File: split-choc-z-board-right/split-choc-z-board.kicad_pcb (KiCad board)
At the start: 2 copper layers, 147.1 x 106.5 mm, 79 parts, among them J1 USB4105-GF-A, J2 USB4105-GF-A, SW1 SW_SPST, SW10 SW_SPST, SW11 SW_SPST, SW12 SW_SPST, SW13 SW_SPST, SW14 SW_SPST, SW15 SW_SPST, SW16 SW_SPST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

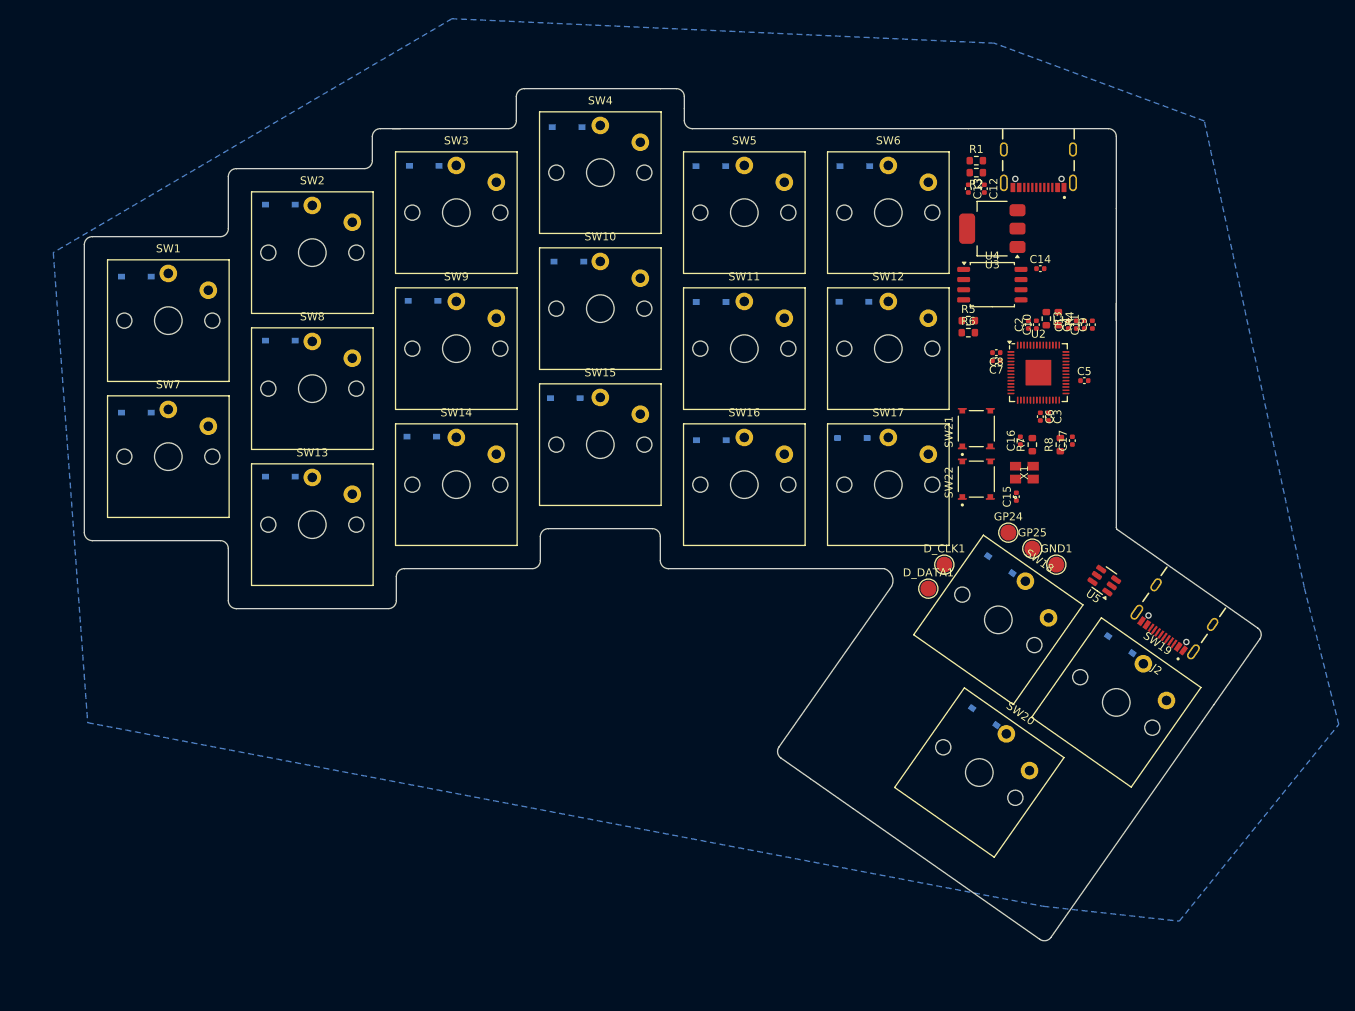
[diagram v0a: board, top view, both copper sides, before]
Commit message: Finalized component placement! 💡
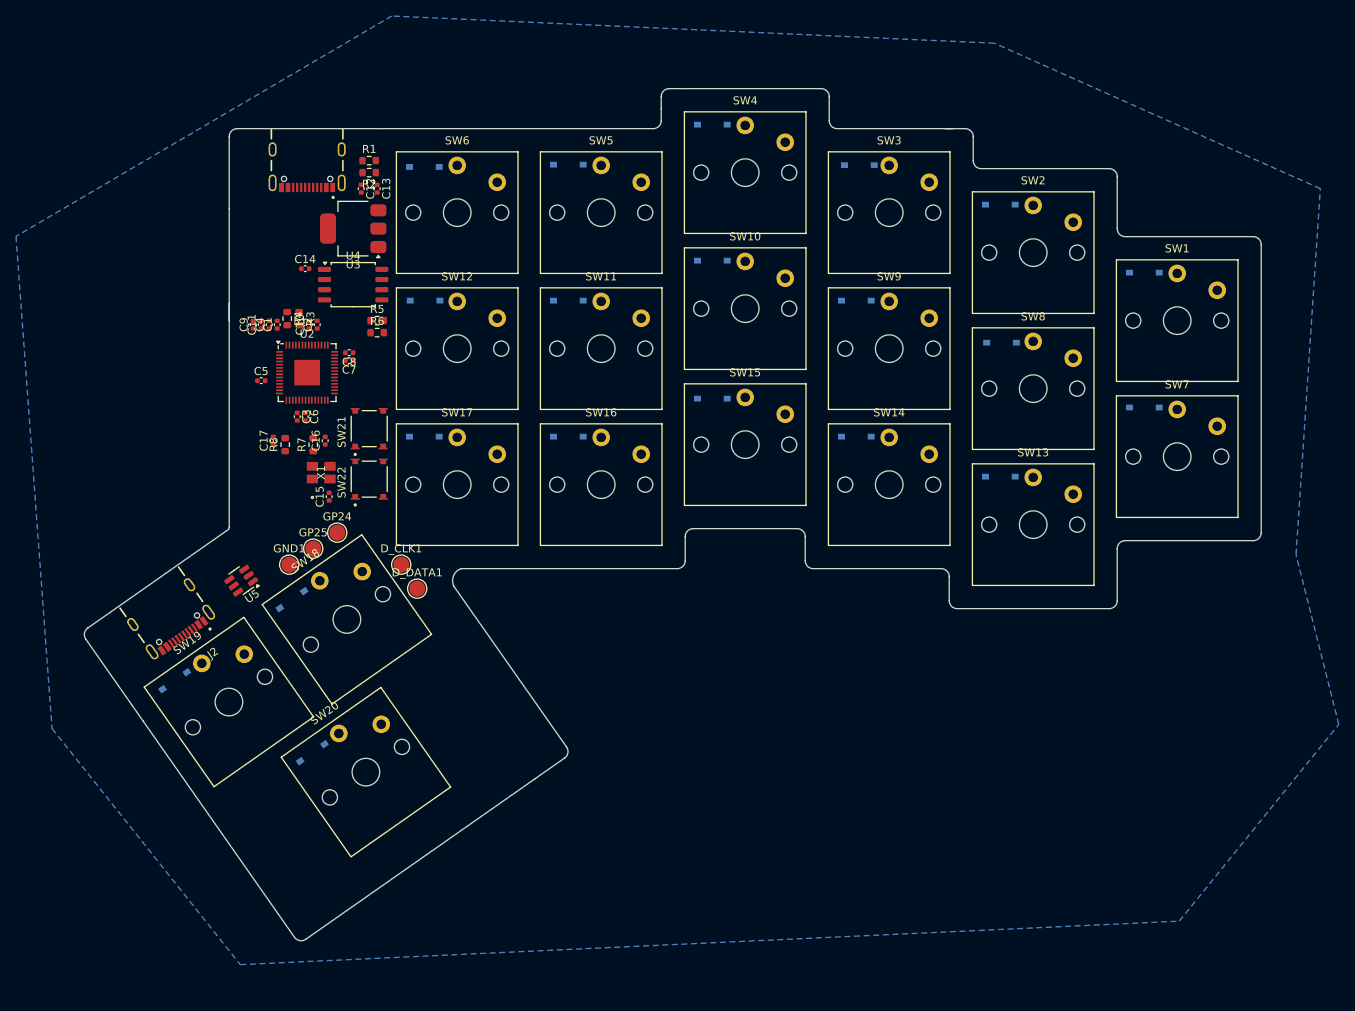
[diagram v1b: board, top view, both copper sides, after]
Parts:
- moved J2 127.9 mm to (35.1, 105.0), turned to -145 degrees
- moved SW1 126.1 mm to (162.1, 69.5)
- moved SW7 126.1 mm to (162.1, 86.5)
- moved D19 118.3 mm to (36.8, 114.5), turned to 35 degrees
- moved SW19 110.9 mm to (43.6, 117.2), turned to 35 degrees
- moved D1 108.3 mm to (158.0, 63.5)
- moved U5 107.9 mm to (45.1, 102.0), turned to -145 degrees
- moved C9 104.9 mm to (46.6, 70.0)
- moved C11 102.9 mm to (47.6, 70.0)
- moved C5 102.9 mm to (47.6, 77.0)
- moved C4 100.9 mm to (48.6, 70.0)
- moved C17 99.9 mm to (49.1, 84.5)
- moved C1 98.9 mm to (49.6, 70.0)
- moved R8 96.9 mm to (50.6, 85.0)
- moved R4 96.4 mm to (50.9, 69.2)
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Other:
- outline, holes or cut-outs redrawn
- board text removed: "Created by Zain Kergaye 4/12/25"
- board text removed: "L"

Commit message: Copied left hand component placement changes to right hand
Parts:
- removed D_CLK1, D_DATA1: TestPoint, TestPoint:TestPoint_Pad_D2.0mm
- added J3: Conn_01x04_Pin, Connector_PinHeader_2.54mm:PinHeader_1x04_P2.54mm_Vertical, F.Cu at (48.7, 88.3)
- added J4: Conn_01x02, Connector_PinHeader_2.54mm:PinHeader_1x02_P2.54mm_Vertical, F.Cu at (46.2, 63.3)
- moved C9 3.54 mm to (47.7, 73.4), turned to 0 degrees
- moved C11 2.36 mm to (47.7, 72.4), turned to 0 degrees
- moved C1 1.92 mm to (47.7, 70.4), turned to 0 degrees
- moved C4 1.63 mm to (47.7, 71.4), turned to 0 degrees
- moved C2 0.84 mm to (53.8, 70.0)
- moved C10 0.74 mm to (52.9, 70.0)
- moved R3 0.69 mm to (51.7, 69.2)
- moved R4 0.69 mm to (50.2, 69.2)
- moved C7 0.54 mm to (58.6, 74.0)
- moved C8 0.54 mm to (58.6, 73.0)
- turned R7 to -90 degrees
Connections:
- J1 pad SH1: GND -> unconnected-(J1-SHELL_GND-PadSH1)
- J1 pad SH2: GND -> unconnected-(J1-SHELL_GND__1-PadSH2)
- J1 pad SH3: GND -> unconnected-(J1-SHELL_GND__2-PadSH3)
- J2 pad SH1: GND -> unconnected-(J2-SHELL_GND-PadSH1)
- J2 pad SH2: GND -> unconnected-(J2-SHELL_GND__1-PadSH2)
- J2 pad SH3: GND -> unconnected-(J2-SHELL_GND__2-PadSH3)

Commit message: Routing right side!
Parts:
- moved C14 12.3 mm to (65.3, 64.5)
- moved C1 11.3 mm to (59.0, 71.0)
- moved C11 11.3 mm to (59.0, 73.0)
- moved C4 11.3 mm to (59.0, 72.0)
- moved C9 11.3 mm to (59.0, 74.0)
- moved C7 10.7 mm to (47.9, 73.8)
- moved C8 10.7 mm to (47.9, 72.8)
- moved C17 8.76 mm to (57.6, 82.3), turned to -90 degrees
- moved R8 6.98 mm to (57.6, 84.9)
- moved R4 5.44 mm to (55.6, 69.6)
- moved R3 2.46 mm to (54.1, 69.6)
- moved C3 2.26 mm to (54.4, 81.5)
- moved C15 2.12 mm to (54.0, 91.6)
- moved C2 1.80 mm to (52.0, 69.9)
- moved R6 1.54 mm to (62.1, 69.5), turned to 180 degrees
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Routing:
- net /Col_4: track 0.00 -> 253.3 mm, vias 0 -> 2
- net /Col_2: track 0.00 -> 251.1 mm, vias 0 -> 2
- net /Col_3: track 0.00 -> 250.1 mm, vias 0 -> 4
- net /Col_1: track 0.00 -> 194.0 mm, vias 0 -> 1
- net /Row_1: track 0.00 -> 161.2 mm, vias 0 -> 3
- net /Row_2: track 0.00 -> 146.9 mm, vias 0 -> 1
- net /Row_4: track 0.00 -> 130.5 mm, vias 0 -> 3
- net /Row_5: track 0.00 -> 112.7 mm, vias 0 -> 1
- net +3V3: track 0.00 -> 94.4 mm, vias 0 -> 4
- net VBUS: track 0.00 -> 90.7 mm, vias 0 -> 5
- net /Row_3: track 0.00 -> 86.6 mm, vias 0 -> 3
- net GND: track 0.00 -> 85.2 mm, vias 0 -> 18
- net /GP24: track 0.00 -> 61.4 mm, vias 0 -> 4
- net /B-B_D-: track 0.00 -> 46.7 mm, vias 0 -> 2
- net /B-B_D+: track 0.00 -> 43.3 mm
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
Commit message: Finished routing right! 👏🏻
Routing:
- net +1V1: track 9.39 -> 45.8 mm, vias 0 -> 4
- net +3V3: track 94.4 -> 127.5 mm, vias 4 -> 7
- net GND: track 85.2 -> 117.3 mm, vias 18 -> 19
- net /QSPI_SS: track 28.7 -> 29.9 mm
- net /QSPI_SD3: track 16.7 -> 17.4 mm
- net /QSPI_SD0: track 17.1 -> 17.8 mm
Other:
- outline, holes or cut-outs redrawn
